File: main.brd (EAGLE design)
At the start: 27.6 x 69.8 mm, 6 parts, among them SW1 1825910-6, SW2 1825910-6

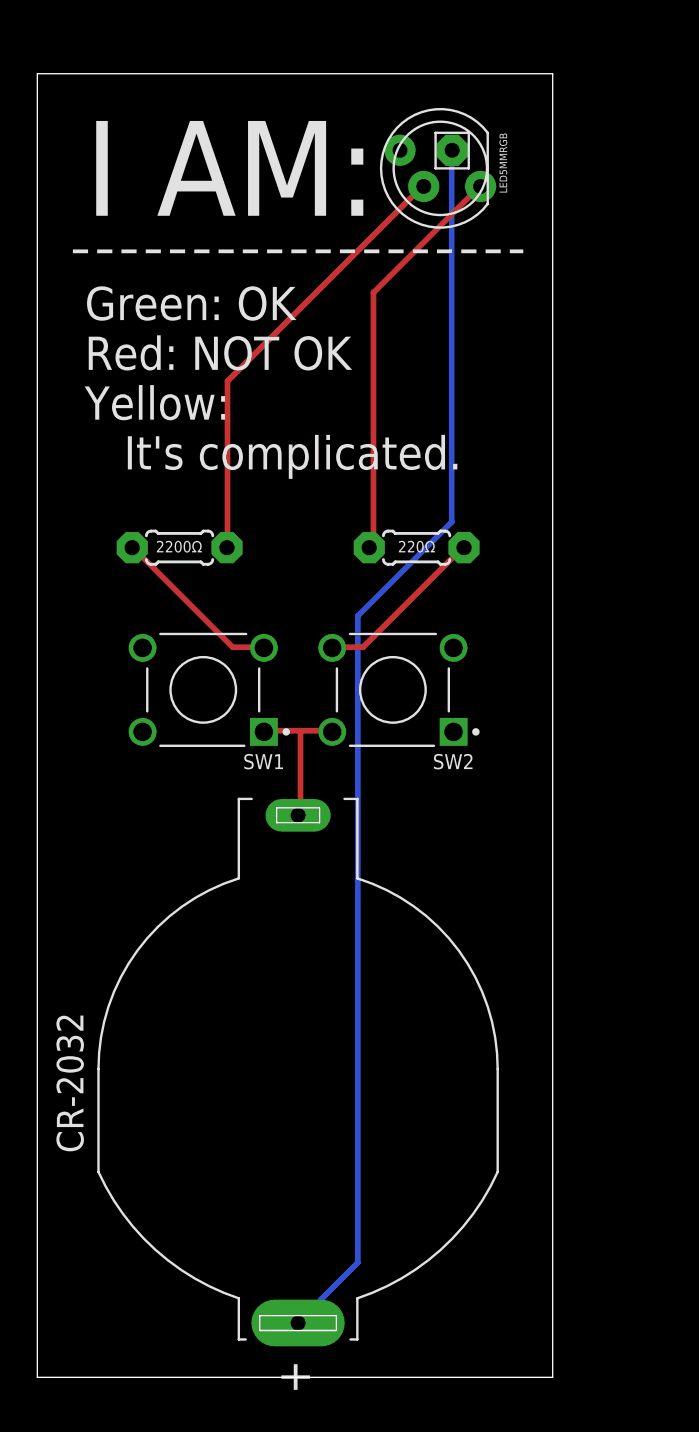
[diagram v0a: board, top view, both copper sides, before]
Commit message: Refactored autorouting with new net class and did DRC
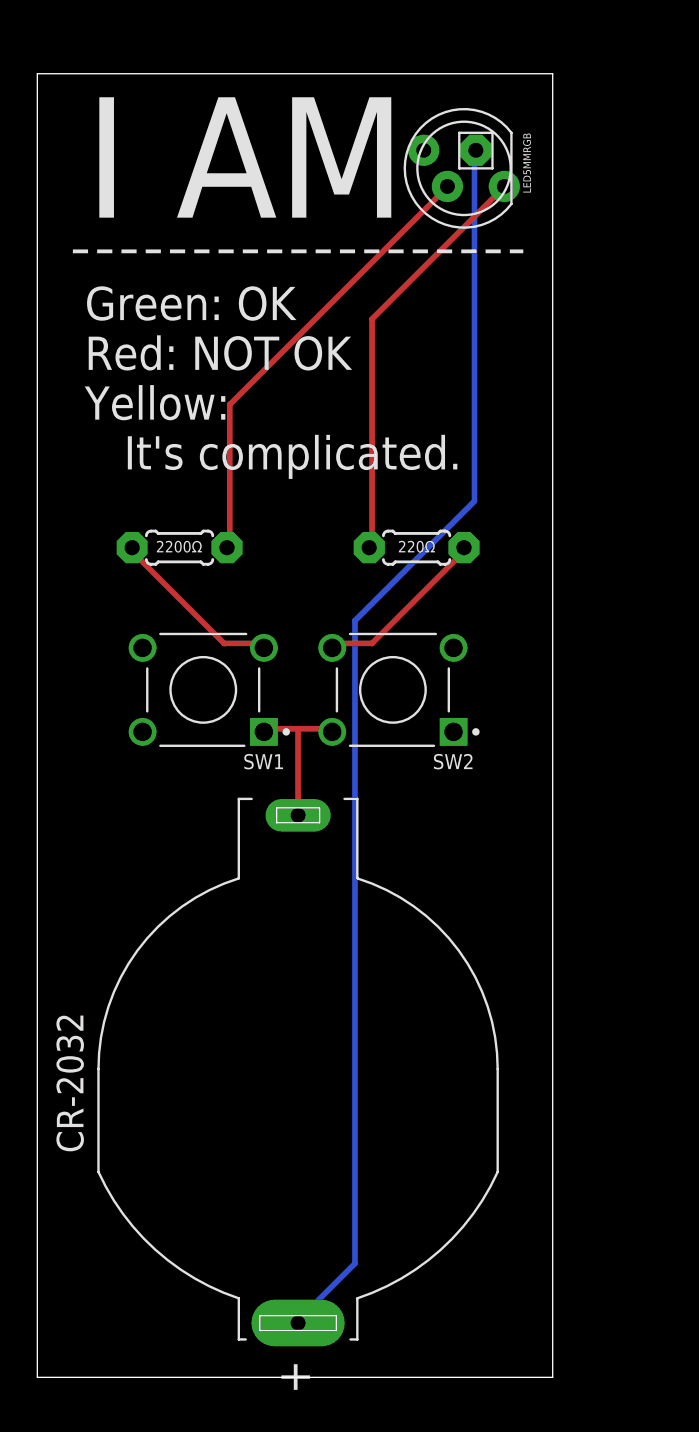
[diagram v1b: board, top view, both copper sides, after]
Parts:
- moved LED5MMRGB 1.27 mm to (24.1, 64.8)
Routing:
- net N$5: track 21.8 -> 22.4 mm
- net N$4: track 23.7 -> 24.3 mm
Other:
- board text added: "I AM"
- board text removed: "I AM:"
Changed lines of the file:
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@@
 <wire x1="28.88" y1="69.84" x2="1.27" y2="69.84" width="0" layer="20"/>
 <wire x1="1.27" y1="69.84" x2="1.27" y2="0" width="0" layer="20"/>
-<text x="3.81" y="67.31" size="5.08" layer="25" font="vector" align="top-left">I AM:</text>
+<text x="3.81" y="68.58" size="6.4516" layer="25" font="vector" align="top-left">I AM</text>
 <text x="3.81" y="58.42" size="1.778" layer="25" font="vector" align="top-left">Green: OK
 Red: NOT OK
@@
 <classes>
 <class number="0" name="default" width="0.3048" drill="0.254">
-<clearance class="0" value="0.254"/>
+<clearance class="0" value="0.3048"/>
 </class>
 </classes>
@@
 <attribute name="PACKAGE" value="DFN-8 Memory Protection Devices" x="29.21" y="44.45" size="1.778" layer="27" rot="R90" display="off"/>
 </element>
-<element name="LED5MMRGB" library="adafruit" package="LED5MMRGB" value="RGBLED_CA-5MM" x="22.86" y="64.77" smashed="yes" rot="R180">
-<attribute name="NAME" x="26.035" y="66.675" size="0.4064" layer="21" rot="R270"/>
+<element name="LED5MMRGB" library="adafruit" package="LED5MMRGB" value="RGBLED_CA-5MM" x="24.13" y="64.77" smashed="yes" rot="R180">
+<attribute name="NAME" x="27.305" y="66.675" size="0.4064" layer="21" rot="R270"/>
 </element>
 <element name="220Ω" library="adafruit" package="0204/5" value="" x="21.59" y="44.45" smashed="yes" rot="R180">
@@
 <contactref element="SW1" pad="1"/>
 <contactref element="SW2" pad="2"/>
-<wire x1="17.0434" y1="34.6456" x2="15.367" y2="34.6456" width="0.3048" layer="1"/>
-<wire x1="15.367" y1="34.6456" x2="13.4112" y2="34.6456" width="0.3048" layer="1"/>
-<wire x1="13.4112" y1="34.6456" x2="13.41" y2="34.58" width="0.3048" layer="1"/>
-<wire x1="17.0434" y1="34.6456" x2="17.07" y2="34.58" width="0.3048" layer="1"/>
-<wire x1="15.367" y1="34.6456" x2="15.367" y2="30.1752" width="0.3048" layer="1"/>
-<wire x1="15.367" y1="30.1752" x2="15.24" y2="30.11" width="0.3048" layer="1"/>
+<wire x1="17.0688" y1="34.7472" x2="15.24" y2="34.7472" width="0.3048" layer="1"/>
+<wire x1="15.24" y1="34.7472" x2="13.4112" y2="34.7472" width="0.3048" layer="1"/>
+<wire x1="13.4112" y1="34.7472" x2="13.41" y2="34.58" width="0.3048" layer="1"/>
+<wire x1="17.0688" y1="34.7472" x2="17.07" y2="34.58" width="0.3048" layer="1"/>
+<wire x1="15.24" y1="34.7472" x2="15.24" y2="30.11" width="0.3048" layer="1"/>
 </signal>
 <signal name="N$4">
 <contactref element="2200Ω" pad="2"/>
 <contactref element="LED5MMRGB" pad="3"/>
-<wire x1="11.4554" y1="53.3654" x2="11.4554" y2="44.704" width="0.3048" layer="1"/>
-<wire x1="21.7932" y1="63.7032" x2="11.4554" y2="53.3654" width="0.3048" layer="1"/>
-<wire x1="11.4554" y1="44.704" x2="11.43" y2="44.45" width="0.3048" layer="1"/>
-<wire x1="21.7932" y1="63.7032" x2="21.971" y2="63.8016" width="0.3048" layer="1"/>
+<wire x1="23.1648" y1="63.7032" x2="11.5824" y2="52.1208" width="0.3048" layer="1"/>
+<wire x1="23.1648" y1="63.7032" x2="23.241" y2="63.8016" width="0.3048" layer="1"/>
+<wire x1="11.5824" y1="52.1208" x2="11.5824" y2="44.5008" width="0.3048" layer="1"/>
+<wire x1="11.5824" y1="44.5008" x2="11.43" y2="44.45" width="0.3048" layer="1"/>
 </signal>
 <signal name="N$5">
 <contactref element="LED5MMRGB" pad="1"/>
 <contactref element="220Ω" pad="2"/>
-<wire x1="19.2786" y1="58.1152" x2="19.2786" y2="44.704" width="0.3048" layer="1"/>
-<wire x1="24.8666" y1="63.7032" x2="19.2786" y2="58.1152" width="0.3048" layer="1"/>
-<wire x1="19.2786" y1="44.704" x2="19.05" y2="44.45" width="0.3048" layer="1"/>
-<wire x1="24.8666" y1="63.7032" x2="25.019" y2="63.8016" width="0.3048" layer="1"/>
+<wire x1="19.2024" y1="56.6928" x2="19.2024" y2="44.5008" width="0.3048" layer="1"/>
+<wire x1="26.2128" y1="63.7032" x2="19.2024" y2="56.6928" width="0.3048" layer="1"/>
+<wire x1="19.2024" y1="44.5008" x2="19.05" y2="44.45" width="0.3048" layer="1"/>
+<wire x1="26.2128" y1="63.7032" x2="26.289" y2="63.8016" width="0.3048" layer="1"/>
 </signal>
 <signal name="N$6">
 <contactref element="LED5MMRGB" pad="2"/>
 <contactref element="CR-2032" pad="P"/>
-<wire x1="15.24" y1="3.048" x2="15.24" y2="2.91" width="0.1524" layer="16"/>
-<wire x1="23.4696" y1="45.8216" x2="23.4696" y2="65.659" width="0.3048" layer="16"/>
-<wire x1="18.4404" y1="40.7924" x2="23.4696" y2="45.8216" width="0.3048" layer="16"/>
-<wire x1="18.4404" y1="6.1468" x2="18.4404" y2="40.7924" width="0.3048" layer="16"/>
-<wire x1="15.367" y1="3.0734" x2="18.4404" y2="6.1468" width="0.3048" layer="16"/>
-<wire x1="23.4696" y1="65.659" x2="23.495" y2="65.7384" width="0.3048" layer="16"/>
-<wire x1="15.367" y1="3.0734" x2="15.24" y2="2.91" width="0.3048" layer="16"/>
+<wire x1="24.6888" y1="46.9392" x2="24.6888" y2="65.532" width="0.3048" layer="16"/>
+<wire x1="18.288" y1="40.5384" x2="24.6888" y2="46.9392" width="0.3048" layer="16"/>
+<wire x1="18.288" y1="6.096" x2="18.288" y2="40.5384" width="0.3048" layer="16"/>
+<wire x1="15.24" y1="3.048" x2="18.288" y2="6.096" width="0.3048" layer="16"/>
+<wire x1="24.6888" y1="65.532" x2="24.765" y2="65.7384" width="0.3048" layer="16"/>
+<wire x1="15.24" y1="3.048" x2="15.24" y2="2.91" width="0.3048" layer="16"/>
 </signal>
 <signal name="N$2">
 <contactref element="2200Ω" pad="1"/>
 <contactref element="SW1" pad="3"/>
-<wire x1="11.7348" y1="39.116" x2="13.1318" y2="39.116" width="0.3048" layer="1"/>
-<wire x1="6.4262" y1="44.4246" x2="11.7348" y2="39.116" width="0.3048" layer="1"/>
-<wire x1="13.1318" y1="39.116" x2="13.41" y2="39.08" width="0.3048" layer="1"/>
-<wire x1="6.4262" y1="44.4246" x2="6.35" y2="44.45" width="0.3048" layer="1"/>
+<wire x1="11.2776" y1="39.3192" x2="13.1064" y2="39.3192" width="0.3048" layer="1"/>
+<wire x1="6.4008" y1="44.196" x2="11.2776" y2="39.3192" width="0.3048" layer="1"/>
+<wire x1="13.1064" y1="39.3192" x2="13.41" y2="39.08" width="0.3048" layer="1"/>
+<wire x1="6.4008" y1="44.196" x2="6.35" y2="44.45" width="0.3048" layer="1"/>
 </signal>
 <signal name="N$3">
 <contactref element="220Ω" pad="1"/>
 <contactref element="SW2" pad="4"/>
-<wire x1="18.7198" y1="39.116" x2="17.3228" y2="39.116" width="0.3048" layer="1"/>
-<wire x1="24.0284" y1="44.4246" x2="18.7198" y2="39.116" width="0.3048" layer="1"/>
-<wire x1="17.3228" y1="39.116" x2="17.07" y2="39.08" width="0.3048" layer="1"/>
-<wire x1="24.0284" y1="44.4246" x2="24.13" y2="44.45" width="0.3048" layer="1"/>
+<wire x1="19.2024" y1="39.3192" x2="17.3736" y2="39.3192" width="0.3048" layer="1"/>
+<wire x1="24.0792" y1="44.196" x2="19.2024" y2="39.3192" width="0.3048" layer="1"/>
+<wire x1="17.3736" y1="39.3192" x2="17.07" y2="39.08" width="0.3048" layer="1"/>
+<wire x1="24.0792" y1="44.196" x2="24.13" y2="44.45" width="0.3048" layer="1"/>
 </signal>
 </signals>
